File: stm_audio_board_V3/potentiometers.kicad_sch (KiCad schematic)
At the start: 6 parts

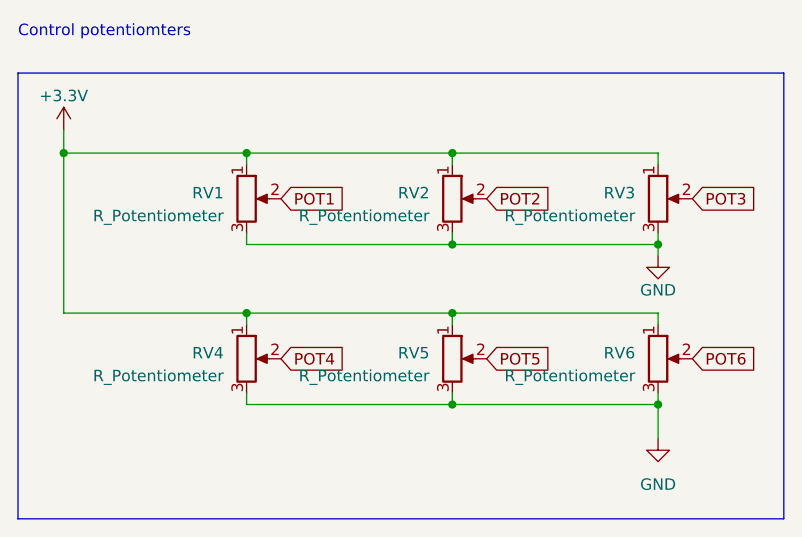
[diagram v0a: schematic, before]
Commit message: Input and output stages are made and assembly started on pcb view
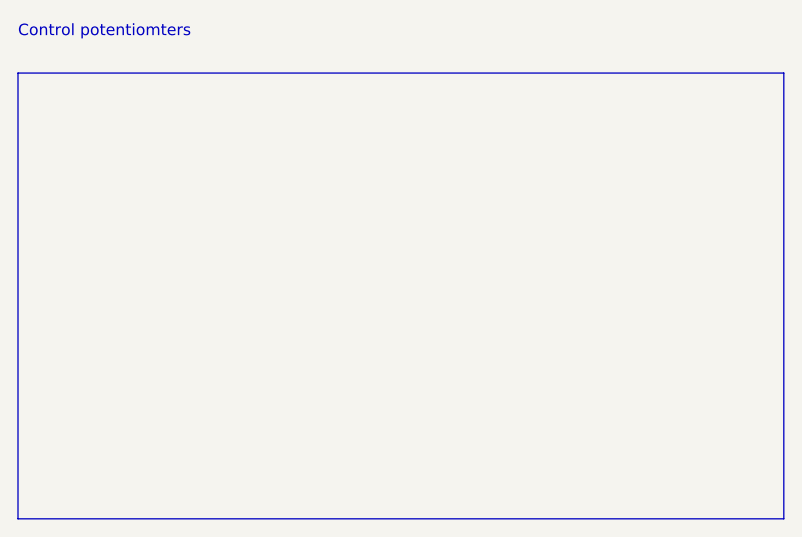
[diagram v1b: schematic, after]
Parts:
- removed RV1, RV2, RV3, RV4, RV5, RV6: R_Potentiometer, Potentiometer_THT:Potentiometer_Omeg_PC16BU_Vertical, symbol Device:R_Potentiometer

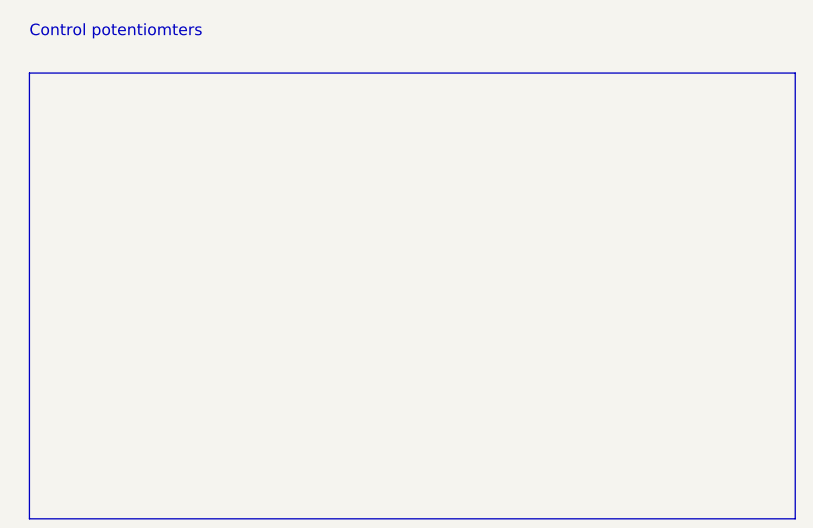
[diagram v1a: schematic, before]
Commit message: Input output connected to codec
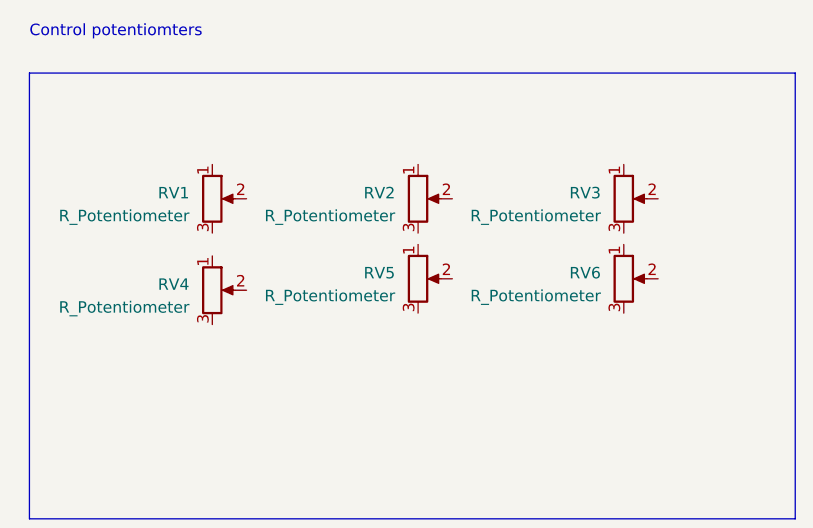
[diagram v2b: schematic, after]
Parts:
- added RV1, RV2, RV3, RV4, RV5, RV6: R_Potentiometer, Potentiometer_THT:Potentiometer_Alps_RK09L_Single_Vertical, symbol Device:R_Potentiometer
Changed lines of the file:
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@@
     (effects (font (size 1.27 1.27)) (justify left bottom))
   )
+  (symbol (lib_id "Device:R_Potentiometer") (at 64.77 48.26 0) (unit 1)
+    (in_bom yes) (on_board yes) (dnp no) (fields_autoplaced)
+    (property "Reference" "RV2" (at 62.23 47.625 0)
+      (effects (font (size 1.27 1.27)) (justify right))
+    )
+    (property "Value" "R_Potentiometer" (at 62.23 50.165 0)
+      (effects (font (size 1.27 1.27)) (justify right))
+    )
+    (property "Footprint" "Potentiometer_THT:Potentiometer_Alps_RK09L_Single_Vertical" (at 64.77 48.26 0)
+      (effects (font (size 1.27 1.27)) hide)
+    )
+    (property "Datasheet" "~" (at 64.77 48.26 0)
+      (effects (font (size 1.27 1.27)) hide)
+    )
+    (property "LINK" "https://hu.mouser.com/ProductDetail/Alps-Alpine/RK09L1240A12?qs=YMSFtX0bdJDG8WU5rH%252BliQ%3D%3D" (at 64.77 48.26 0)
+      (effects (font (size 1.27 1.27)) hide)
+    )
+    (property "Field5" "" (at 64.77 48.26 0)
+      (effects (font (size 1.27 1.27)) hide)
+    )
+    (pin "1")
+    (pin "2")
+    (pin "3")
+    (instances
+      (project "stm_audio_board_V3"
+        (path "/6997cf63-2615-4e49-9471-e7da1b6bae71/f3a016e9-328b-49a9-9257-9482800e0ff5"
+          (reference "RV2") (unit 1)
+        )
+      )
+    )
+  )
+  (symbol (lib_id "Device:R_Potentiometer") (at 87.63 57.15 0) (unit 1)
+    (in_bom yes) (on_board yes) (dnp no) (fields_autoplaced)
+    (property "Reference" "RV6" (at 85.09 56.515 0)
+      (effects (font (size 1.27 1.27)) (justify right))
+    )
+    (property "Value" "R_Potentiometer" (at 85.09 59.055 0)
+      (effects (font (size 1.27 1.27)) (justify right))
+    )
+    (property "Footprint" "Potentiometer_THT:Potentiometer_Alps_RK09L_Single_Vertical" (at 87.63 57.15 0)
+      (effects (font (size 1.27 1.27)) hide)
+    )
+    (property "Datasheet" "~" (at 87.63 57.15 0)
+      (effects (font (size 1.27 1.27)) hide)
+    )
+    (property "LINK" "https://hu.mouser.com/ProductDetail/Alps-Alpine/RK09L1240A12?qs=YMSFtX0bdJDG8WU5rH%252BliQ%3D%3D" (at 87.63 57.15 0)
+      (effects (font (size 1.27 1.27)) hide)
+    )
+    (property "Field5" "" (at 87.63 57.15 0)
+      (effects (font (size 1.27 1.27)) hide)
+    )
+    (pin "1")
+    (pin "2")
+    (pin "3")
+    (instances
+      (project "stm_audio_board_V3"
+        (path "/6997cf63-2615-4e49-9471-e7da1b6bae71/f3a016e9-328b-49a9-9257-9482800e0ff5"
+          (reference "RV6") (unit 1)
+        )
+      )
+    )
+  )
+  (symbol (lib_id "Device:R_Potentiometer") (at 41.91 48.26 0) (unit 1)
+    (in_bom yes) (on_board yes) (dnp no) (fields_autoplaced)
+    (property "Reference" "RV1" (at 39.37 47.625 0)
+      (effects (font (size 1.27 1.27)) (justify right))
+    )
+    (property "Value" "R_Potentiometer" (at 39.37 50.165 0)
+      (effects (font (size 1.27 1.27)) (justify right))
+    )
+    (property "Footprint" "Potentiometer_THT:Potentiometer_Alps_RK09L_Single_Vertical" (at 41.91 48.26 0)
+      (effects (font (size 1.27 1.27)) hide)
+    )
+    (property "Datasheet" "~" (at 41.91 48.26 0)
+      (effects (font (size 1.27 1.27)) hide)
+    )
+    (property "LINK" "https://hu.mouser.com/ProductDetail/Alps-Alpine/RK09L1240A12?qs=YMSFtX0bdJDG8WU5rH%252BliQ%3D%3D" (at 41.91 48.26 0)
+      (effects (font (size 1.27 1.27)) hide)
+    )
+    (property "Field5" "" (at 41.91 48.26 0)
+      (effects (font (size 1.27 1.27)) hide)
+    )
+    (pin "1")
+    (pin "2")
+    (pin "3")
+    (instances
+      (project "stm_audio_board_V3"
+        (path "/6997cf63-2615-4e49-9471-e7da1b6bae71/f3a016e9-328b-49a9-9257-9482800e0ff5"
+          (reference "RV1") (unit 1)
+        )
+      )
+    )
+  )
+  (symbol (lib_id "Device:R_Potentiometer") (at 87.63 48.26 0) (unit 1)
+    (in_bom yes) (on_board yes) (dnp no) (fields_autoplaced)
+    (property "Reference" "RV3" (at 85.09 47.625 0)
+      (effects (font (size 1.27 1.27)) (justify right))
+    )
+    (property "Value" "R_Potentiometer" (at 85.09 50.165 0)
+      (effects (font (size 1.27 1.27)) (justify right))
+    )
+    (property "Footprint" "Potentiometer_THT:Potentiometer_Alps_RK09L_Single_Vertical" (at 87.63 48.26 0)
+      (effects (font (size 1.27 1.27)) hide)
+    )
+    (property "Datasheet" "~" (at 87.63 48.26 0)
+      (effects (font (size 1.27 1.27)) hide)
+    )
+    (property "LINK" "https://hu.mouser.com/ProductDetail/Alps-Alpine/RK09L1240A12?qs=YMSFtX0bdJDG8WU5rH%252BliQ%3D%3D" (at 87.63 48.26 0)
+      (effects (font (size 1.27 1.27)) hide)
+    )
+    (property "Field5" "" (at 87.63 48.26 0)
+      (effects (font (size 1.27 1.27)) hide)
+    )
+    (pin "1")
+    (pin "2")
+    (pin "3")
+    (instances
+      (project "stm_audio_board_V3"
+        (path "/6997cf63-2615-4e49-9471-e7da1b6bae71/f3a016e9-328b-49a9-9257-9482800e0ff5"
+          (reference "RV3") (unit 1)
+        )
+      )
+    )
+  )
+  (symbol (lib_id "Device:R_Potentiometer") (at 64.77 57.15 0) (unit 1)
+    (in_bom yes) (on_board yes) (dnp no) (fields_autoplaced)
+    (property "Reference" "RV5" (at 62.23 56.515 0)
+      (effects (font (size 1.27 1.27)) (justify right))
+    )
+    (property "Value" "R_Potentiometer" (at 62.23 59.055 0)
+      (effects (font (size 1.27 1.27)) (justify right))
+    )
+    (property "Footprint" "Potentiometer_THT:Potentiometer_Alps_RK09L_Single_Vertical" (at 64.77 57.15 0)
+      (effects (font (size 1.27 1.27)) hide)
+    )
+    (property "Datasheet" "~" (at 64.77 57.15 0)
+      (effects (font (size 1.27 1.27)) hide)
+    )
+    (property "LINK" "https://hu.mouser.com/ProductDetail/Alps-Alpine/RK09L1240A12?qs=YMSFtX0bdJDG8WU5rH%252BliQ%3D%3D" (at 64.77 57.15 0)
+      (effects (font (size 1.27 1.27)) hide)
+    )
+    (property "Field5" "" (at 64.77 57.15 0)
+      (effects (font (size 1.27 1.27)) hide)
+    )
+    (pin "1")
+    (pin "2")
+    (pin "3")
+    (instances
+      (project "stm_audio_board_V3"
+        (path "/6997cf63-2615-4e49-9471-e7da1b6bae71/f3a016e9-328b-49a9-9257-9482800e0ff5"
+          (reference "RV5") (unit 1)
+        )
+      )
+    )
+  )
+  (symbol (lib_id "Device:R_Potentiometer") (at 41.91 58.42 0) (unit 1)
+    (in_bom yes) (on_board yes) (dnp no) (fields_autoplaced)
+    (property "Reference" "RV4" (at 39.37 57.785 0)
+      (effects (font (size 1.27 1.27)) (justify right))
+    )
+    (property "Value" "R_Potentiometer" (at 39.37 60.325 0)
+      (effects (font (size 1.27 1.27)) (justify right))
+    )
+    (property "Footprint" "Potentiometer_THT:Potentiometer_Alps_RK09L_Single_Vertical" (at 41.91 58.42 0)
+      (effects (font (size 1.27 1.27)) hide)
+    )
+    (property "Datasheet" "~" (at 41.91 58.42 0)
+      (effects (font (size 1.27 1.27)) hide)
+    )
+    (property "LINK" "https://hu.mouser.com/ProductDetail/Alps-Alpine/RK09L1240A12?qs=YMSFtX0bdJDG8WU5rH%252BliQ%3D%3D" (at 41.91 58.42 0)
+      (effects (font (size 1.27 1.27)) hide)
+    )
+    (property "Field5" "" (at 41.91 58.42 0)
+      (effects (font (size 1.27 1.27)) hide)
+    )
+    (pin "1")
+    (pin "2")
+    (pin "3")
+    (instances
+      (project "stm_audio_board_V3"
+        (path "/6997cf63-2615-4e49-9471-e7da1b6bae71/f3a016e9-328b-49a9-9257-9482800e0ff5"
+          (reference "RV4") (unit 1)
+        )
+      )
+    )
+  )
 )

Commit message: minor changes
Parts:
- added C14 (x6): 100n, Capacitor_SMD:C_0603_1608Metric, symbol Device:C_Small
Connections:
- net +3.3V: now reaches RV2.1
- net +3.3V: now also RV1.1, RV3.1, RV4.1, RV5.1, RV6.1
- net POT3: now reaches RV2.2
- net POT3: now also C14.1
- net GND: now reaches RV2.3
- net GND: now also RV1.3, RV3.3, RV4.3, RV5.3, RV6.3, C14.2, C14.2, C14.2, C14.2, C14.2, C14.2
- net POT6: now reaches RV6.2
- net POT6: now also C14.1
- net POT1: now reaches RV1.2
- net POT1: now also C14.1
- net POT5: now reaches RV3.2
- net POT5: now also C14.1
- net POT4: now reaches RV5.2
- net POT4: now also C14.1
- net POT2: now reaches RV4.2
- net POT2: now also C14.1
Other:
- note removed: "Control potentiomters"
- moved on the sheet: RV2, RV3, RV4, RV5, RV6

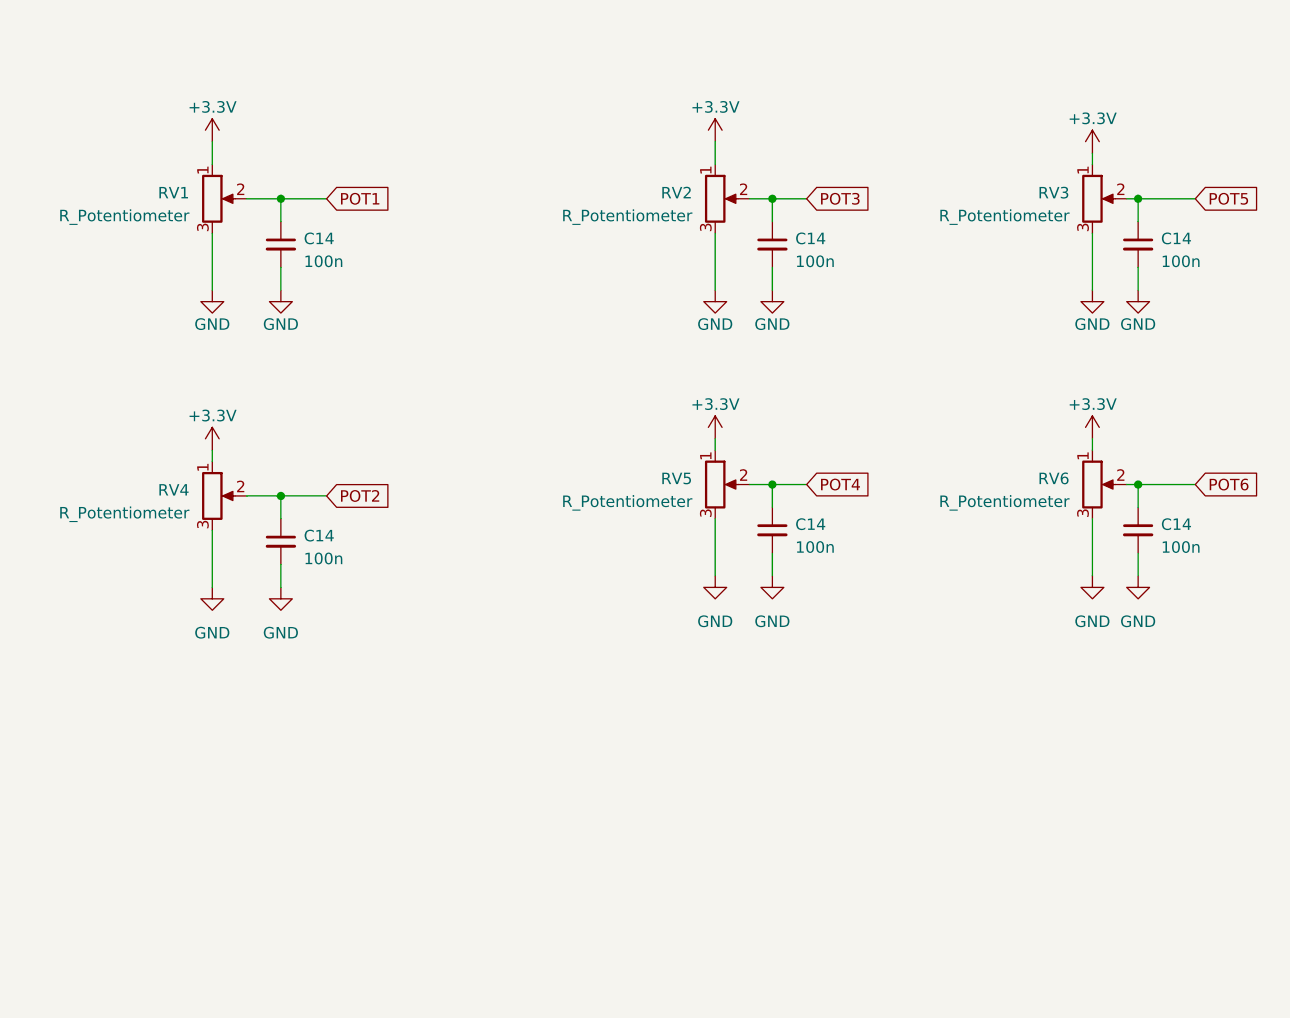
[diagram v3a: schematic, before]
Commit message: +-12 DCDC added
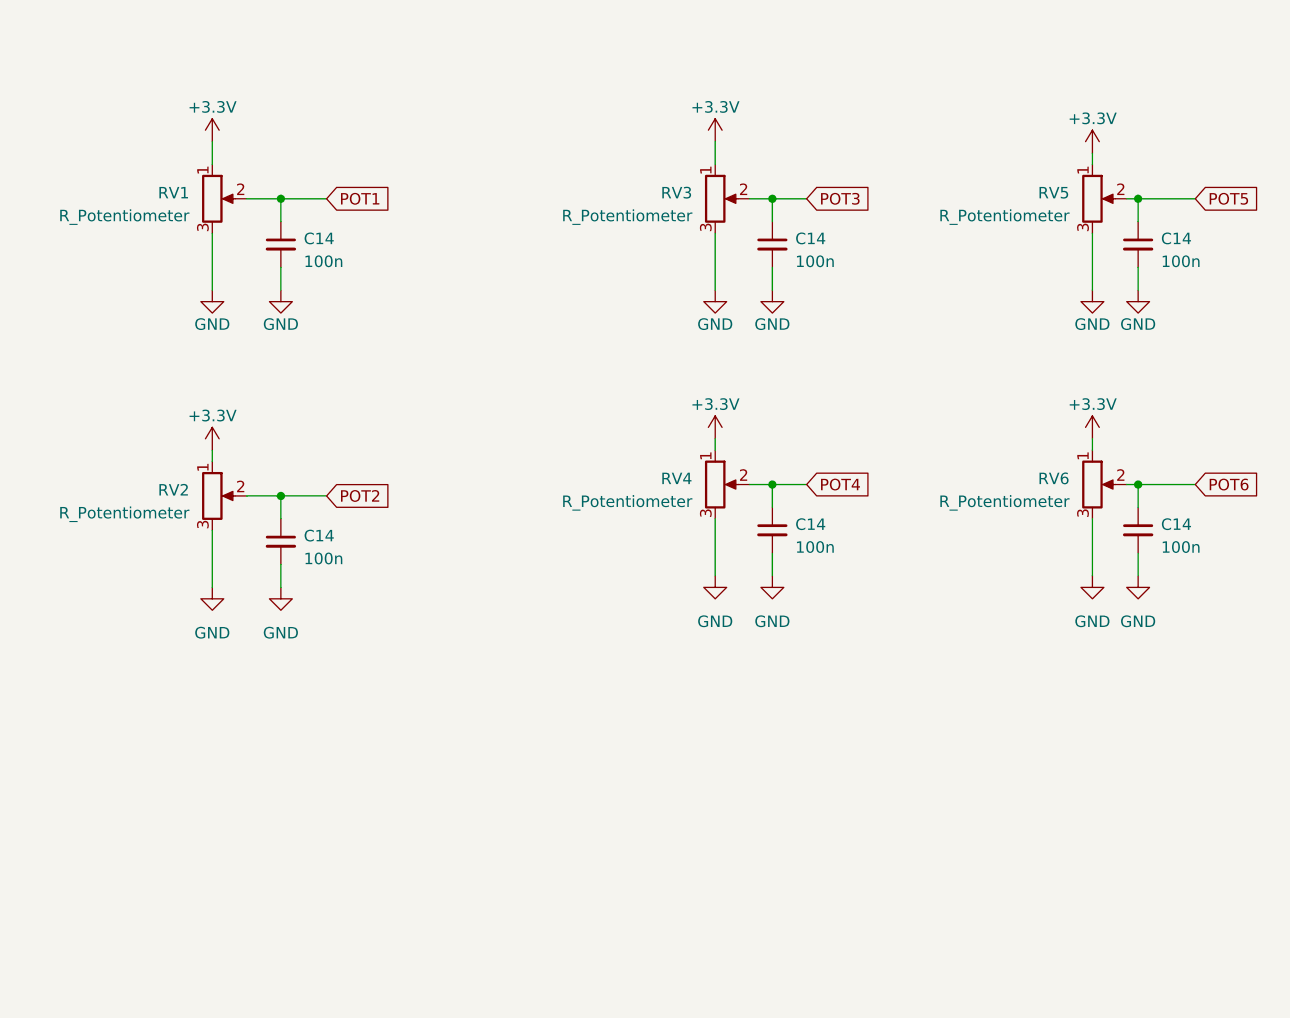
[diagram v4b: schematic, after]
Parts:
- renumbered RV4 to RV2, RV2 to RV3, RV5 to RV4, RV3 to RV5
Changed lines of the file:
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@@
   (symbol (lib_id "Device:R_Potentiometer") (at 97.79 48.26 0) (unit 1)
     (in_bom yes) (on_board yes) (dnp no) (fields_autoplaced)
-    (property "Reference" "RV2" (at 95.25 47.625 0)
+    (property "Reference" "RV3" (at 95.25 47.625 0)
       (effects (font (size 1.27 1.27)) (justify right))
     )
@@
   (symbol (lib_id "Device:R_Potentiometer") (at 139.7 48.26 0) (unit 1)
     (in_bom yes) (on_board yes) (dnp no) (fields_autoplaced)
-    (property "Reference" "RV3" (at 137.16 47.625 0)
+    (property "Reference" "RV5" (at 137.16 47.625 0)
       (effects (font (size 1.27 1.27)) (justify right))
     )
@@
   (symbol (lib_id "Device:R_Potentiometer") (at 97.79 80.01 0) (unit 1)
     (in_bom yes) (on_board yes) (dnp no) (fields_autoplaced)
-    (property "Reference" "RV5" (at 95.25 79.375 0)
+    (property "Reference" "RV4" (at 95.25 79.375 0)
       (effects (font (size 1.27 1.27)) (justify right))
     )
@@
   (symbol (lib_id "Device:R_Potentiometer") (at 41.91 81.28 0) (unit 1)
     (in_bom yes) (on_board yes) (dnp no) (fields_autoplaced)
-    (property "Reference" "RV4" (at 39.37 80.645 0)
-      (effects (font (size 1.27 1.27)) (justify right))
-    )
+    (property "Reference" "RV2" (at 39.37 80.645 0)
+      (effects (font (size 1.27 1.27)) (justify right))
+    )

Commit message: PCB design is finished
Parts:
- added C14: 100n, Capacitor_SMD:C_0603_1608Metric, symbol Device:C_Small
- added J14: External_POT, Connector_Audio:Jack_6.35mm_Neutrik_NMJ6HCD2_Horizontal, symbol Connector_Audio:AudioJack3_Ground_SwitchTR
- added R9: 220R, Resistor_SMD:R_0603_1608Metric, symbol Device:R
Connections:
- net +3.3V: now also J14.T
- net GND: now also C14.2, J14.RN, J14.S
- new net: J14.R, R9.2
- new net EXT_POT_ADC: C14.1, R9.1
